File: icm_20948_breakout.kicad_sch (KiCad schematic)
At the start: 16 parts, among them J1 Conn_01x07, U1 SN74LVC2T45YZP, U2 SN74LVC2T45YZP, U3 SN74LVC1T45DRL, U4 TLV70018DCKR, U5 ICM-20948

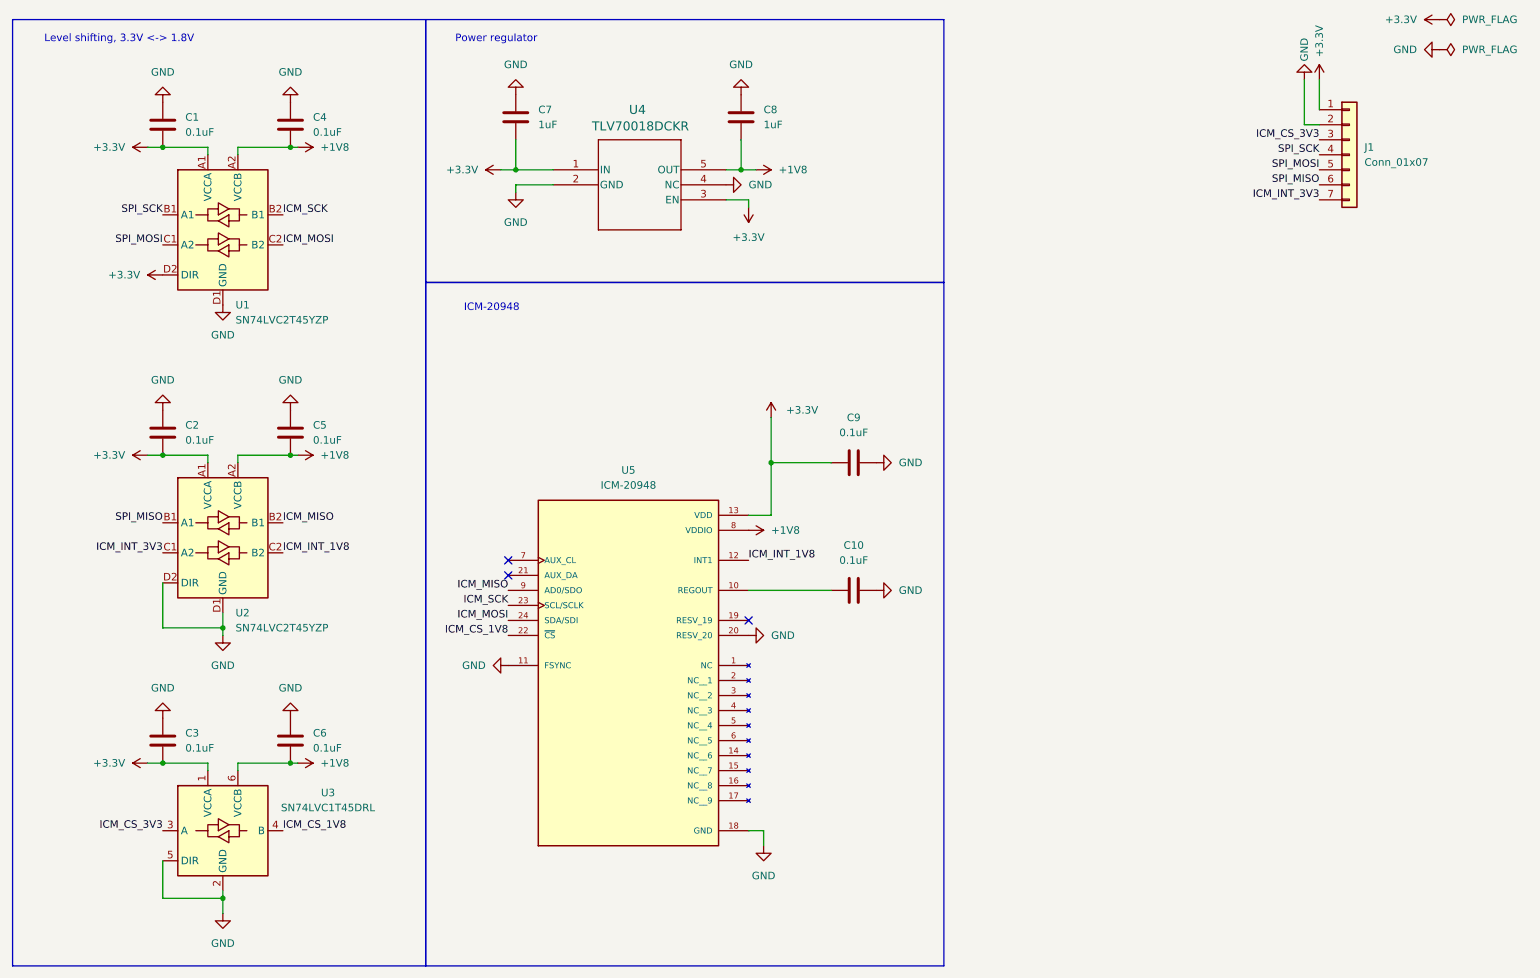
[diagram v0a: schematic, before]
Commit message: Revised footprints and re-designed PCB
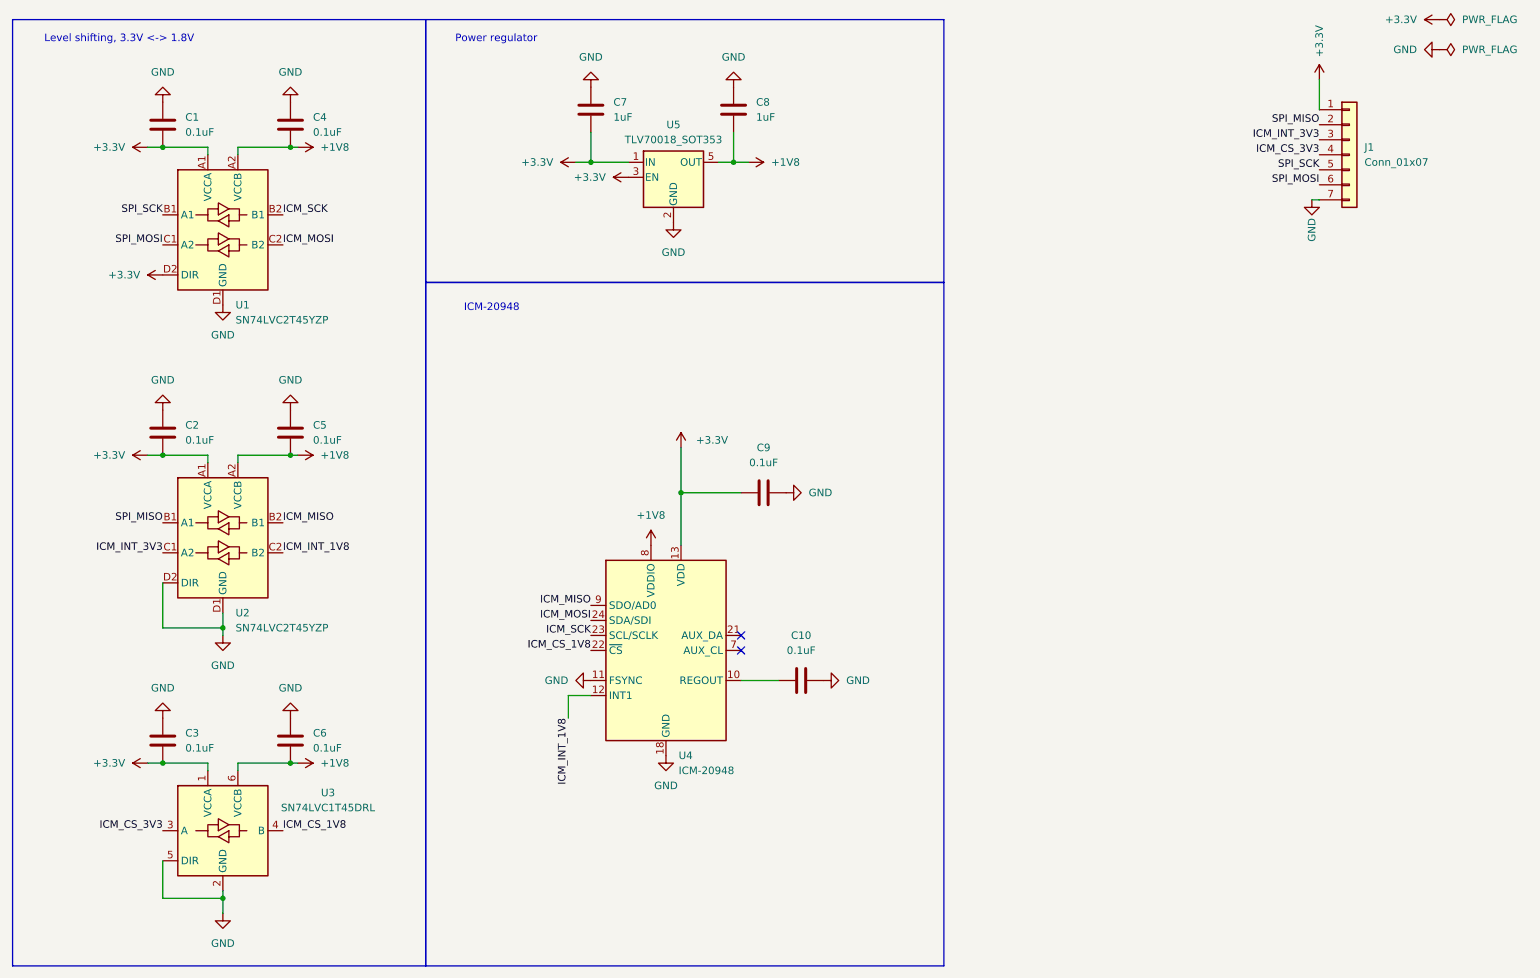
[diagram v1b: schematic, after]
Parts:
- removed U4: TLV70018DCKR, Texas-Instruments-TLV70018DCKR:DCK5, symbol Texas-Instruments-TLV70018DCKR:TLV70018DCKR
- removed U5: ICM-20948, ICM_20948:QFN40P300X300X105-24N, symbol ICM-20948:ICM-20948
- added U4: ICM-20948, Sensor_Motion:InvenSense_QFN-24_3x3mm_P0.4mm, symbol Sensor_Motion:ICM-20948
- added U5: TLV70018_SOT353, Package_TO_SOT_SMD:SOT-353_SC-70-5, symbol Regulator_Linear:TLV70018_SOT353
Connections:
- net +1V8: now also U4.8 (VDDIO), U5.5 (OUT)
- net +3.3V: now also U4.13 (VDD), U5.1 (IN), U5.3 (EN)
- net GND: now also J1.7 (Pin_7), U4.11 (FSYNC), U4.18 (GND), U4.20 (GND), U5.2 (GND); no longer J1.2 (Pin_2)
- net ICM_CS_1V8: now also U4.22 (~{CS})
- net ICM_CS_3V3: now also J1.4 (Pin_4); no longer J1.3 (Pin_3)
- net ICM_INT_1V8: now also U4.12 (INT1)
- net ICM_INT_3V3: now also J1.3 (Pin_3); no longer J1.7 (Pin_7)
- net ICM_MISO: now also U4.9 (SDO/AD0)
- net ICM_MOSI: now also U4.24 (SDA/SDI)
- net ICM_SCK: now also U4.23 (SCL/SCLK)
- net SPI_MISO: now also J1.2 (Pin_2); no longer J1.6 (Pin_6)
- net SPI_MOSI: now also J1.6 (Pin_6); no longer J1.5 (Pin_5)
- net SPI_SCK: now also J1.5 (Pin_5); no longer J1.4 (Pin_4)
- net at C10.1: now also U4.10 (REGOUT)
- no-connect marks 3 -> 2

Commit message: tried out automatic production file generation
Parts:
- C1, C10, C2, C3, C4, C5, C6, C9: LCSC (none) -> C1525
- C7, C8: LCSC (none) -> C88945
- J1: LCSC (none) -> C492406
- U1, U2: LCSC (none) -> C913828
- U3: LCSC (none) -> C352970
- U4: LCSC (none) -> C726001
- U5: LCSC (none) -> C133796
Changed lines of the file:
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@@
+			)
+		)
+		(property "LCSC" "C1525"
+			(at 66.04 41.91 0)
+			(effects
+				(font
+					(size 1.27 1.27)
+				)
+				(hide yes)
 			)
 		)
@@
 			)
 		)
+		(property "LCSC" "C88945"
+			(at 116.84 39.37 0)
+			(effects
+				(font
+					(size 1.27 1.27)
+				)
+				(hide yes)
+			)
+		)
 		(pin "2"
 		)
@@
 			)
 		)
+		(property "LCSC" "C913828"
+			(at 54.61 59.69 0)
+			(effects
+				(font
+					(size 1.27 1.27)
+				)
+				(hide yes)
+			)
+		)
 		(pin "A2"
 		)
@@
 			)
 		)
+		(property "LCSC" "C352970"
+			(at 54.61 161.29 0)
+			(effects
+				(font
+					(size 1.27 1.27)
+				)
+				(hide yes)
+			)
+		)
 		(pin "6"
 		)
@@
 			)
 		)
+		(property "LCSC" "C1525"
+			(at 44.45 41.91 0)
+			(effects
+				(font
+					(size 1.27 1.27)
+				)
+				(hide yes)
+			)
+		)
 		(pin "2"
 		)
@@
 			)
 		)
-		(property "Field5" ""
+		(property "LCSC" "C1525"
 			(at 146.05 104.14 90)
 			(effects
@@
 			)
 		)
+		(property "LCSC" "C913828"
+			(at 54.61 111.76 0)
+			(effects
+				(font
+					(size 1.27 1.27)
+				)
+				(hide yes)
+			)
+		)
 		(pin "A2"
 		)
@@
 			)
 		)
+		(property "LCSC" "C1525"
+			(at 44.45 93.98 0)
+			(effects
+				(font
+					(size 1.27 1.27)
+				)
+				(hide yes)
+			)
+		)
 		(pin "2"
 		)
@@
 			)
 		)
+		(property "LCSC" "C1525"
+			(at 66.04 146.05 0)
+			(effects
+				(font
+					(size 1.27 1.27)
+				)
+				(hide yes)
+			)
+		)
 		(pin "1"
 		)
@@
 			)
 		)
+		(property "LCSC" "C133796"
+			(at 130.81 50.8 0)
+			(effects
+				(font
+					(size 1.27 1.27)
+				)
+				(hide yes)
+			)
+		)
 		(pin "1"
 		)
@@
 			)
 		)
+		(property "LCSC" "C726001"
+			(at 129.54 130.81 0)
+			(effects
+				(font
+					(size 1.27 1.27)
+				)
+				(hide yes)
+			)
+		)
 		(pin "16"
 		)
@@
 			)
 		)
+		(property "LCSC" "C1525"
+			(at 44.45 146.05 0)
+			(effects
+				(font
+					(size 1.27 1.27)
+				)
+				(hide yes)
+			)
+		)
 		(pin "2"
 		)
@@
 			)
 		)
+		(property "LCSC" "C1525"
+			(at 152.4 135.89 90)
+			(effects
+				(font
+					(size 1.27 1.27)
+				)
+				(hide yes)
+			)
+		)
 		(pin "2"
 		)
@@
 			)
 		)
+		(property "LCSC" "C1525"
+			(at 66.04 93.98 0)
+			(effects
+				(font
+					(size 1.27 1.27)
+				)
+				(hide yes)
+			)
+		)
 		(pin "1"
 		)
@@
 			)
 		)
+		(property "LCSC" "C88945"
+			(at 140.97 39.37 0)
+			(effects
+				(font
+					(size 1.27 1.27)
+				)
+				(hide yes)
+			)
+		)
 		(pin "2"
 		)
@@
 			(at 245.11 46.99 0)
 			(effects
+				(font
+					(size 1.27 1.27)
+				)
+				(hide yes)
+			)
+		)
+		(property "LCSC" "C492406"
+			(at 245.11 46.99 0)
+			(effects
